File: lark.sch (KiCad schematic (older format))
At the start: 30 parts, among them J1 CONN1, J11 CONN1, J3 Conn_01x05-Connector_Generic, J6 Conn_01x05-Connector_Generic, U6 BMI088

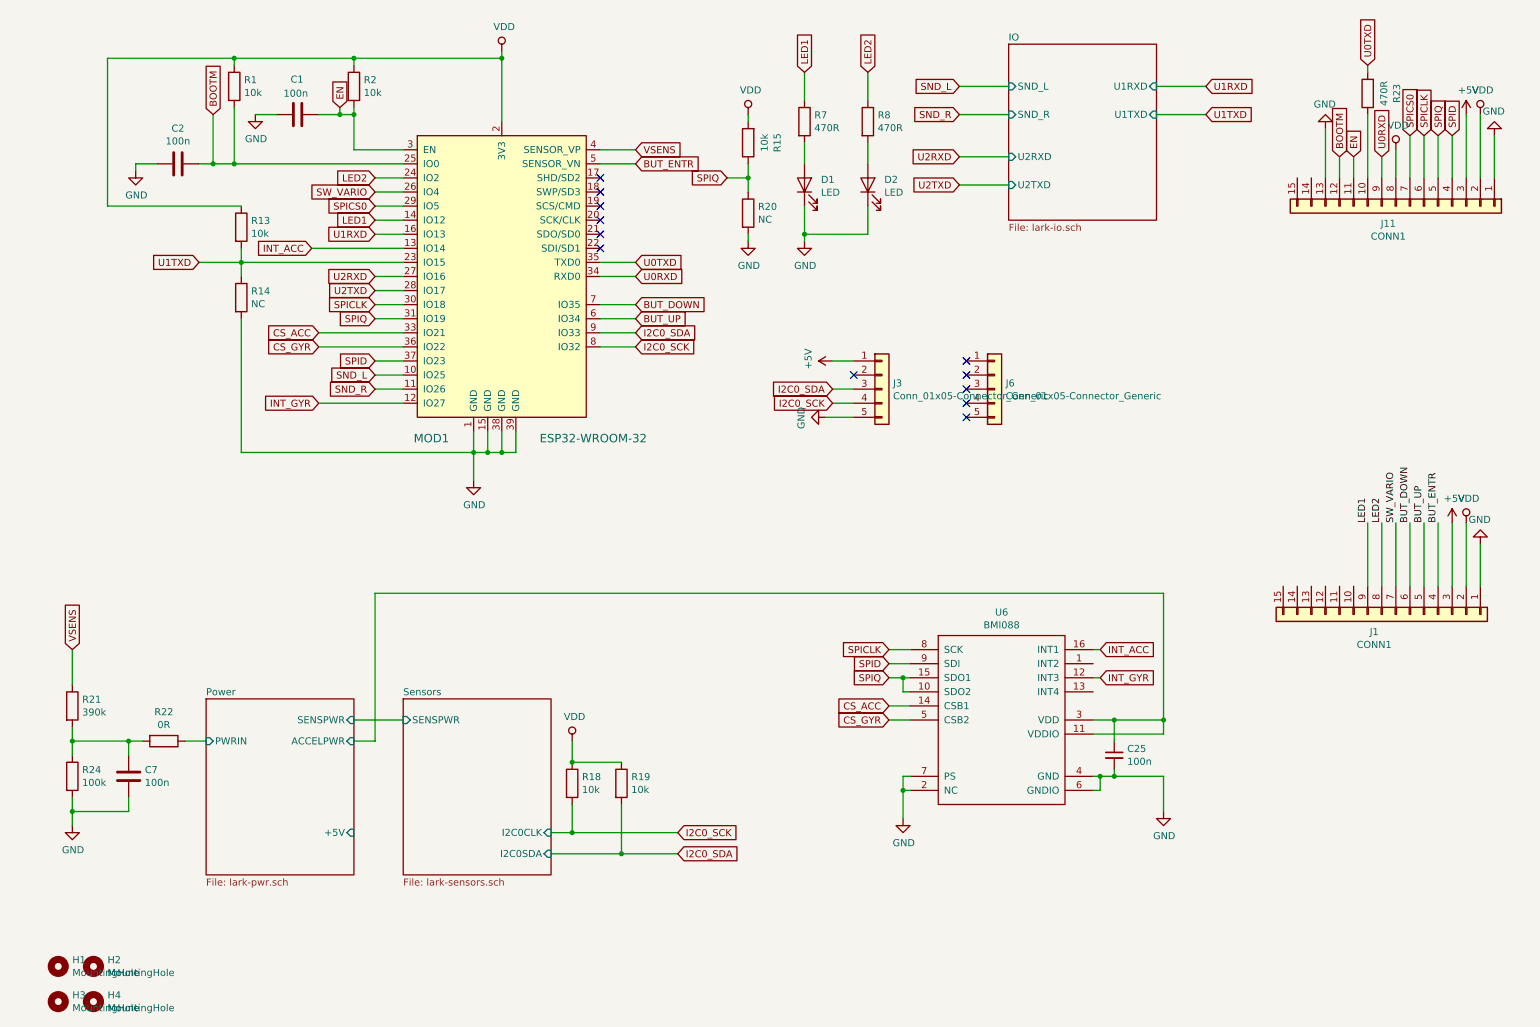
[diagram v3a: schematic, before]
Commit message: connect BMI088 INT lines
They will be set to open-drain mode, so one interrupt pin on the ESP32
can be used for both.
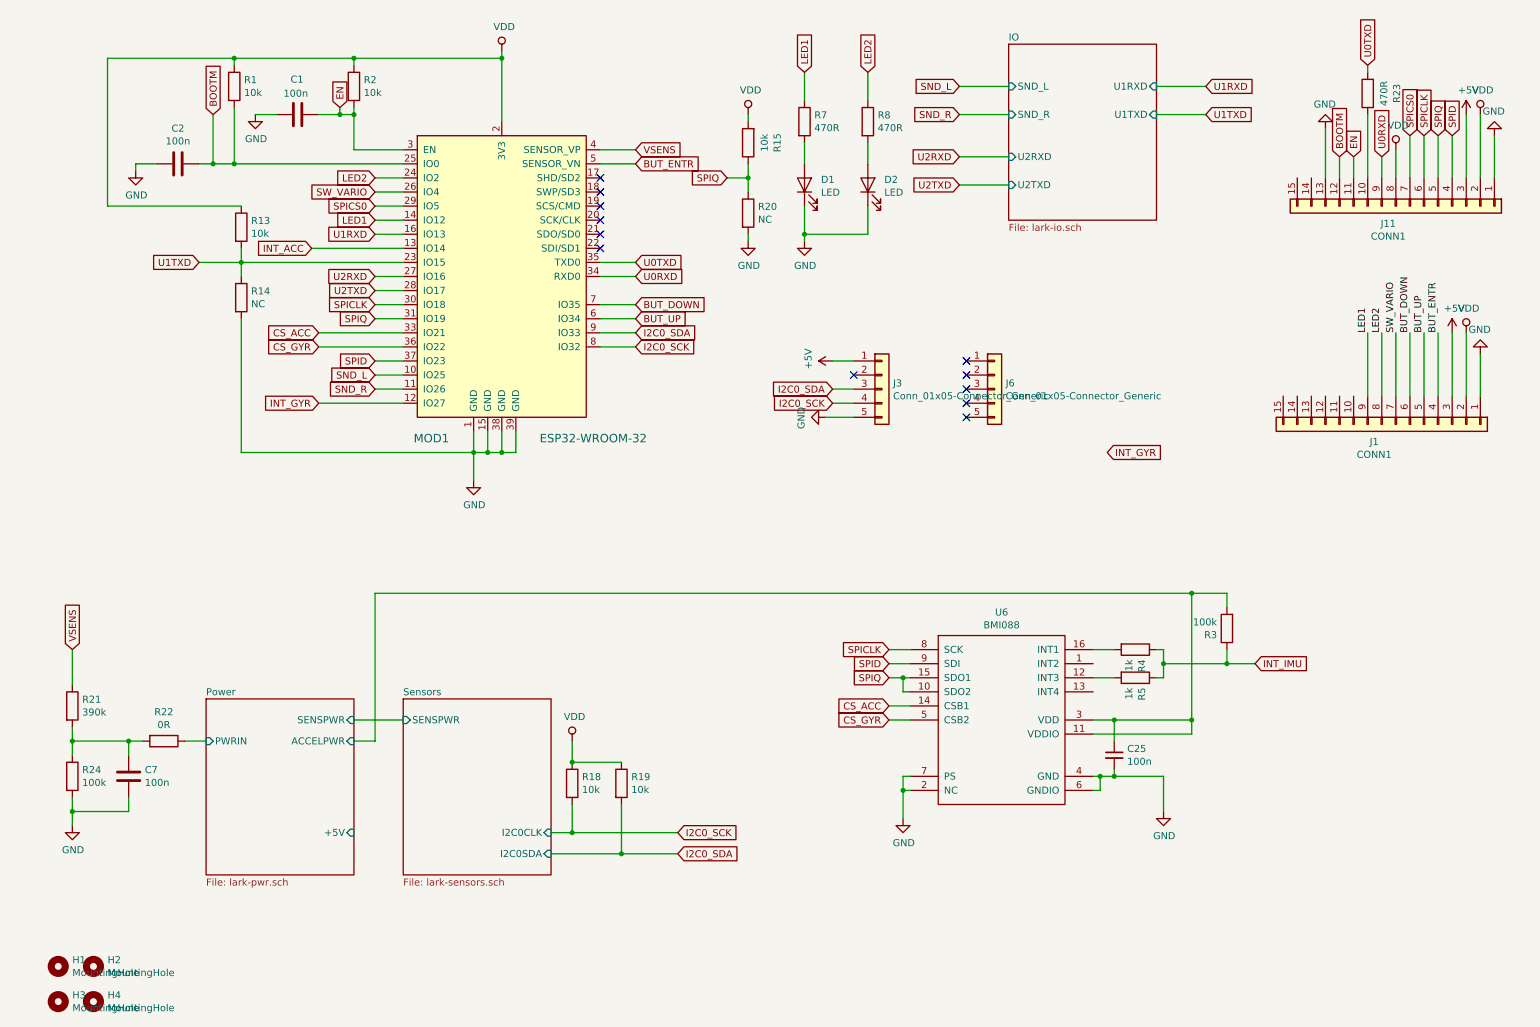
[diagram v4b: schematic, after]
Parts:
- added R3: 100k, Resistor_SMD:R_0805_2012Metric_Pad1.15x1.40mm_HandSolder, symbol lark-rescue:R-Device
- added R4, R5: 1k, Resistor_SMD:R_0805_2012Metric_Pad1.15x1.40mm_HandSolder, symbol lark-rescue:R-Device
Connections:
- net INT_ACC: no longer U6.16 (INT1)
- net INT_GYR: no longer U6.12 (INT3)
- net Power/ACCELPWR: now also R3.2
- new net: R5.2, U6.12 (INT3)
- new net: R4.2, U6.16 (INT1)
- new net INT_IMU: R3.1, R4.1, R5.1
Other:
- moved on the sheet: J1
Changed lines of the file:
@@
 $EndComp
 Wire Wire Line
-	8650 5550 8650 5450
-Connection ~ 8650 5450
+	8850 5550 8850 5450
+Connection ~ 8850 5450
 $Comp
 L Device:C_Small C25
@@
 Connection ~ 8300 5450
 Wire Wire Line
-	8300 5450 8650 5450
+	8300 5450 8850 5450
 Wire Wire Line
 	8150 5850 8200 5850
@@
 Connection ~ 8300 5850
 Wire Wire Line
-	8650 4550 8650 5450
+	8850 4550 8850 5450
 Wire Wire Line
 	6850 5850 6800 5850
@@
 	6800 5950 6800 6150
 Connection ~ 6800 5950
-Wire Wire Line
-	8150 4950 8200 4950
-Wire Wire Line
-	8150 5150 8200 5150
-Text GLabel 8200 4950 2    50   Input ~ 0
-INT_ACC
-Text GLabel 8200 5150 2    50   Input ~ 0
+Text GLabel 9300 5050 2    50   Input ~ 0
+INT_IMU
+Text GLabel 8250 3550 2    50   Input ~ 0
 INT_GYR
 Wire Wire Line
@@
 SPIQ
 Wire Wire Line
-	8650 4550 3050 4550
+	8850 4550 3050 4550
 Wire Wire Line
 	3050 4550 3050 5600
@@
 	3050 5600 2900 5600
 Wire Wire Line
-	10900 4500 10900 4200
-Wire Wire Line
-	10800 4500 10800 4050
-Wire Wire Line
-	10700 4500 10700 4050
-Wire Wire Line
-	10600 4500 10600 4050
-Wire Wire Line
-	10500 4500 10500 4050
+	10900 3150 10900 2850
+Wire Wire Line
+	10800 3150 10800 2700
+Wire Wire Line
+	10700 3150 10700 2700
+Wire Wire Line
+	10600 3150 10600 2700
+Wire Wire Line
+	10500 3150 10500 2700
 $Comp
 L lark-rescue:GND-power #PWR0118
 U 1 1 5CADB2D3
-P 10900 4200
-F 0 "#PWR0118" H 10900 3950 50  0001 C CNN
-F 1 "GND" H 10905 4027 50  0000 C CNN
-F 2 "" H 10900 4200 50  0001 C CNN
-F 3 "" H 10900 4200 50  0001 C CNN
-	1    10900 4200
+P 10900 2850
+F 0 "#PWR0118" H 10900 2600 50  0001 C CNN
+F 1 "GND" H 10905 2677 50  0000 C CNN
+F 2 "" H 10900 2850 50  0001 C CNN
+F 3 "" H 10900 2850 50  0001 C CNN
+	1    10900 2850
 	-1   0    0    1
 $EndComp
@@
 L lark-rescue:VDD-power #PWR0119
 U 1 1 5CADBF21
-P 10800 4050
-F 0 "#PWR0119" H 10800 3900 50  0001 C CNN
-F 1 "VDD" H 10817 4223 50  0000 C CNN
-F 2 "" H 10800 4050 50  0001 C CNN
-F 3 "" H 10800 4050 50  0001 C CNN
-	1    10800 4050
+P 10800 2700
+F 0 "#PWR0119" H 10800 2550 50  0001 C CNN
+F 1 "VDD" H 10817 2873 50  0000 C CNN
+F 2 "" H 10800 2700 50  0001 C CNN
+F 3 "" H 10800 2700 50  0001 C CNN
+	1    10800 2700
 	1    0    0    -1
 $EndComp
@@
 L lark-rescue:+5V-power #PWR0120
 U 1 1 5CAE7419
-P 10700 4050
-F 0 "#PWR0120" H 10700 3900 50  0001 C CNN
-F 1 "+5V" H 10715 4223 50  0000 C CNN
-F 2 "" H 10700 4050 50  0001 C CNN
-F 3 "" H 10700 4050 50  0001 C CNN
-	1    10700 4050
-	1    0    0    -1
-$EndComp
-Wire Wire Line
-	10400 4500 10400 4050
-Wire Wire Line
-	10300 4500 10300 4050
-Text Label 10300 4050 1    50   ~ 0
+P 10700 2700
+F 0 "#PWR0120" H 10700 2550 50  0001 C CNN
+F 1 "+5V" H 10715 2873 50  0000 C CNN
+F 2 "" H 10700 2700 50  0001 C CNN
+F 3 "" H 10700 2700 50  0001 C CNN
+	1    10700 2700
+	1    0    0    -1
+$EndComp
+Wire Wire Line
+	10400 3150 10400 2700
+Wire Wire Line
+	10300 3150 10300 2700
+Text Label 10300 2700 1    50   ~ 0
 SW_VARIO
-Text Label 10400 4050 1    50   ~ 0
+Text Label 10400 2700 1    50   ~ 0
 BUT_DOWN
-Text Label 10500 4050 1    50   ~ 0
+Text Label 10500 2700 1    50   ~ 0
 BUT_UP
-Text Label 10600 4050 1    50   ~ 0
+Text Label 10600 2700 1    50   ~ 0
 BUT_ENTR
 $Comp
@@
 L Connector_Generic:Conn_01x15 J1
 U 1 1 5C9CFD13
-P 10200 4700
-F 0 "J1" V 10324 4646 50  0000 C CNN
-F 1 "CONN1" V 10415 4646 50  0000 C CNN
-F 2 "Connector_PinHeader_2.54mm:PinHeader_1x15_P2.54mm_Vertical" H 10200 4700 50  0001 C CNN
-F 3 "~" H 10200 4700 50  0001 C CNN
-	1    10200 4700
+P 10200 3350
+F 0 "J1" V 10324 3296 50  0000 C CNN
+F 1 "CONN1" V 10415 3296 50  0000 C CNN
+F 2 "Connector_PinHeader_2.54mm:PinHeader_1x15_P2.54mm_Vertical" H 10200 3350 50  0001 C CNN
+F 3 "~" H 10200 3350 50  0001 C CNN
+	1    10200 3350
 	0    1    1    0
 $EndComp
@@
 BUT_ENTR
 Wire Wire Line
-	8150 5550 8650 5550
+	8150 5550 8850 5550
 Wire Wire Line
 	8300 5850 8650 5850
 Wire Wire Line
-	10200 4500 10200 4050
-Wire Wire Line
-	10100 4500 10100 4050
-Text Label 10100 4050 1    50   ~ 0
+	10200 3150 10200 2700
+Wire Wire Line
+	10100 3150 10100 2700
+Text Label 10100 2700 1    50   ~ 0
 LED1
-Text Label 10200 4050 1    50   ~ 0
+Text Label 10200 2700 1    50   ~ 0
 LED2
 NoConn ~ 7250 2900
@@
 	1    0    0    -1
 $EndComp
+$Comp
+L lark-rescue:R-Device R4
+U 1 1 5C942AEC
+P 8450 4950
+F 0 "R4" H 8520 4996 50  0000 L CNN
+F 1 "1k" H 8520 4905 50  0000 L CNN
+F 2 "Resistor_SMD:R_0805_2012Metric_Pad1.15x1.40mm_HandSolder" V 8380 4950 50  0001 C CNN
+F 3 "~" H 8450 4950 50  0001 C CNN
+	1    8450 4950
+	0    1    1    0
+$EndComp
+$Comp
+L lark-rescue:R-Device R5
+U 1 1 5C942BE7
+P 8450 5150
+F 0 "R5" H 8520 5196 50  0000 L CNN
+F 1 "1k" H 8520 5105 50  0000 L CNN
+F 2 "Resistor_SMD:R_0805_2012Metric_Pad1.15x1.40mm_HandSolder" V 8380 5150 50  0001 C CNN
+F 3 "~" H 8450 5150 50  0001 C CNN
+	1    8450 5150
+	0    1    1    0
+$EndComp
+Wire Wire Line
+	8150 5150 8300 5150
+Wire Wire Line
+	8150 4950 8300 4950
+Wire Wire Line
+	8600 4950 8650 4950
+Wire Wire Line
+	8650 4950 8650 5050
+Wire Wire Line
+	8650 5150 8600 5150
+Wire Wire Line
+	8650 5050 9100 5050
+Connection ~ 8650 5050
+Wire Wire Line
+	8650 5050 8650 5150
+$Comp
+L lark-rescue:R-Device R3
+U 1 1 5C9664D7
+P 9100 4800
+F 0 "R3" H 9170 4846 50  0000 L CNN
+F 1 "100k" H 9170 4755 50  0000 L CNN
+F 2 "Resistor_SMD:R_0805_2012Metric_Pad1.15x1.40mm_HandSolder" V 9030 4800 50  0001 C CNN
+F 3 "~" H 9100 4800 50  0001 C CNN
+	1    9100 4800
+	-1   0    0    1
+$EndComp
+Wire Wire Line
+	9100 5050 9100 4950
+Connection ~ 9100 5050
+Wire Wire Line
+	9100 5050 9300 5050
+Wire Wire Line
+	9100 4650 9100 4550
+Wire Wire Line
+	8850 4550 9100 4550
+Connection ~ 8850 4550
 $EndSCHEMATC

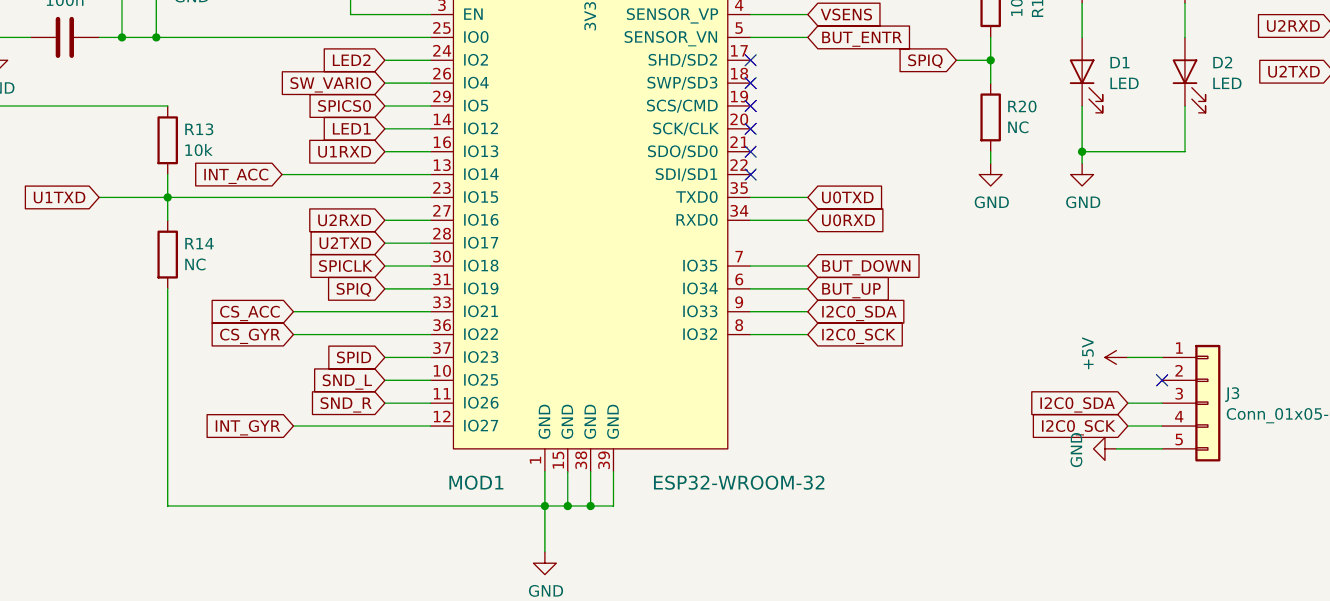
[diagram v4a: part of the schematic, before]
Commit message: connect SENS_INT and IMU_INT to ESP
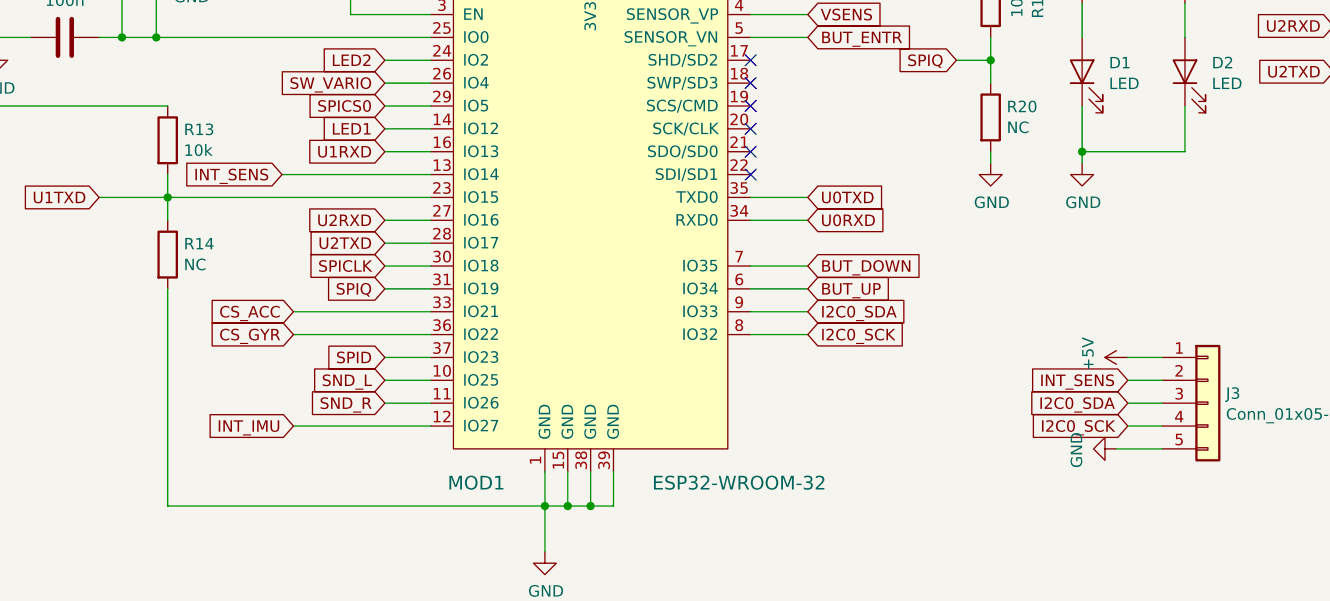
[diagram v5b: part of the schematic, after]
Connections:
- net INT_ACC is gone; now on net INT_SENS: MOD1.13 (IO14)
- net INT_GYR: no longer MOD1.12 (IO27)
- net INT_IMU: now also MOD1.12 (IO27)
- net INT_SENS: now reaches J3.2 (Pin_2)
- no-connect marks 12 -> 11
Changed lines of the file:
@@
 Wire Wire Line
 	2650 3200 3250 3200
+Text GLabel 2600 2100 0    50   Input ~ 0
+INT_SENS
 Text GLabel 2650 3200 0    50   Input ~ 0
-INT_GYR
-Text GLabel 2600 2100 0    50   Input ~ 0
-INT_ACC
+INT_IMU
 $Comp
 L lark-rescue:VDD-power #PWR0107
@@
 	0    -1   -1   0
 $EndComp
-NoConn ~ 6450 3000
 Wire Wire Line
 	6250 3300 6450 3300
@@
 	8850 4550 9100 4550
 Connection ~ 8850 4550
+Wire Wire Line
+	6450 3000 6300 3000
+Text GLabel 6300 3000 0    50   Input ~ 0
+INT_SENS
 $EndSCHEMATC
